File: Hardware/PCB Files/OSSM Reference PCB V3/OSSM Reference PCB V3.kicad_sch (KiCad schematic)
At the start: 2 parts

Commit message: Improved documentation and silkscreen
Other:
- company: (none) -> Research & Desire
- title: (none) -> OSSM!
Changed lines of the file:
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@@
 	(generator_version "8.0")
 	(paper "A4")
+	(title_block
+		(title "OSSM!")
+		(date "2024-08-21")
+		(rev "V3.0 Beta 1")
+		(company "Research & Desire")
+	)
 	(no_connect
 		(at 243.84 133.35)

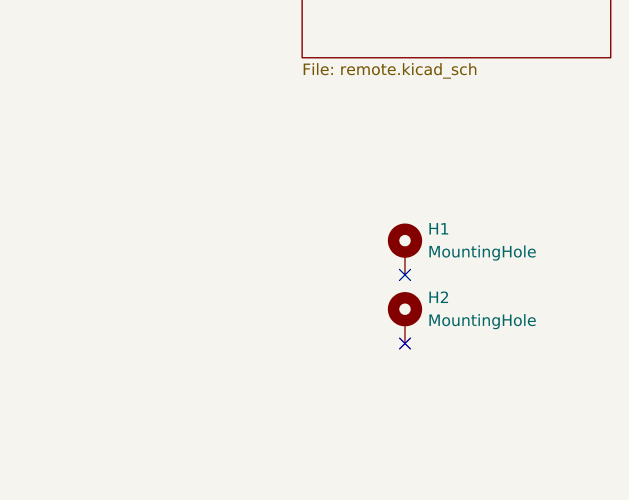
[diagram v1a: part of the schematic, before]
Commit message: Last double check before ordering
Add Test points and Resistor Part numbers
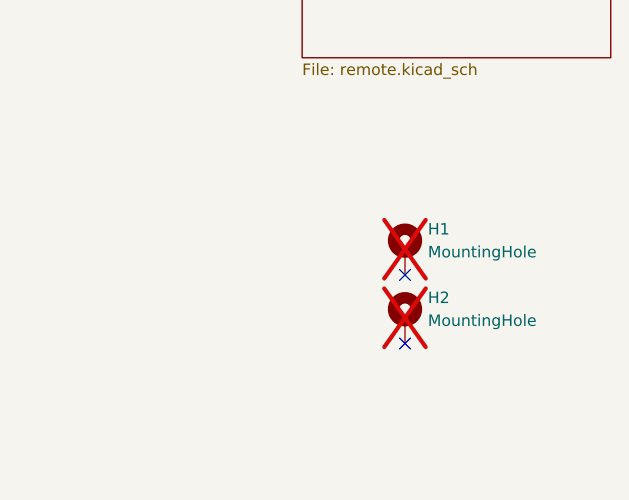
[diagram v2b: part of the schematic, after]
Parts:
- H1, H2: now not fitted
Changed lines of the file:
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@@
 		(in_bom no)
 		(on_board yes)
-		(dnp no)
+		(dnp yes)
 		(fields_autoplaced yes)
 		(property "Reference" "H1"
@@
 		(in_bom no)
 		(on_board yes)
-		(dnp no)
+		(dnp yes)
 		(fields_autoplaced yes)
 		(property "Reference" "H2"
